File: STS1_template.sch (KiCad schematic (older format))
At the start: 9 parts, among them U1 coordinate_system

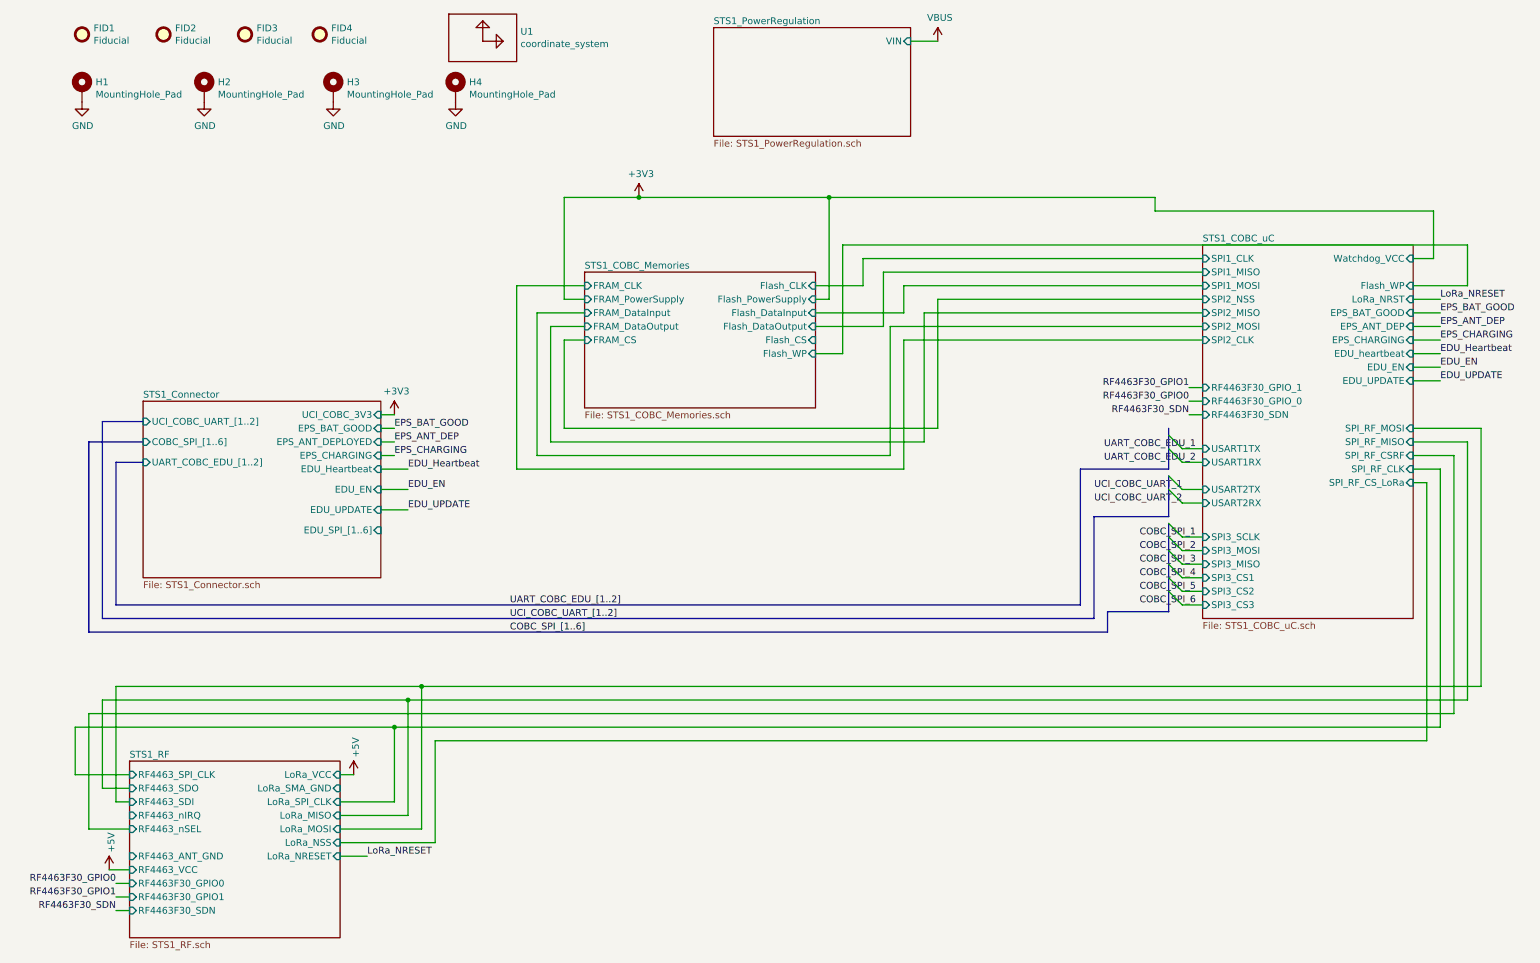
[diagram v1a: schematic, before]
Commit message: added powerplane + testpoints + some debugging
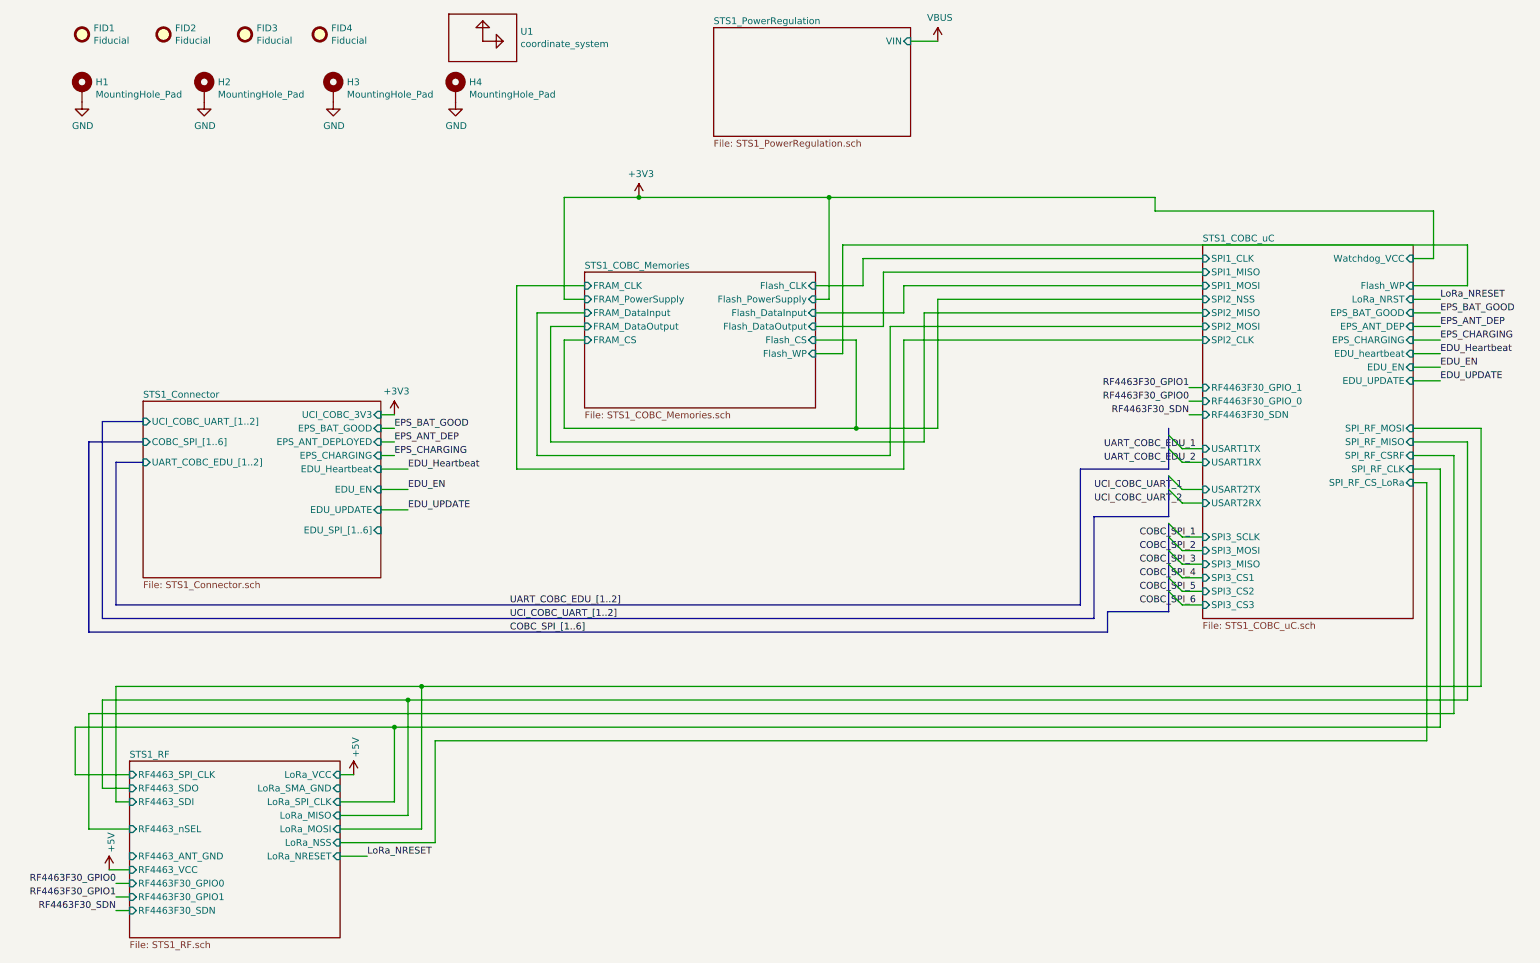
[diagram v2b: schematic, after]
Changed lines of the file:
@@
 F9 "RF4463_ANT_GND" I L 1050 6750 50
 F10 "RF4463_nSEL" I L 1050 6550 50
-F11 "RF4463_nIRQ" I L 1050 6450 50
-F12 "RF4463_SDI" I L 1050 6350 50
-F13 "RF4463_SDO" I L 1050 6250 50
-F14 "RF4463_SPI_CLK" I L 1050 6150 50
-F15 "RF4463F30_GPIO0" I L 1050 6950 50
-F16 "RF4463F30_GPIO1" I L 1050 7050 50
-F17 "LoRa_NRESET" I R 2600 6750 50
-F18 "RF4463F30_SDN" I L 1050 7150 50
+F11 "RF4463_SDI" I L 1050 6350 50
+F12 "RF4463_SDO" I L 1050 6250 50
+F13 "RF4463_SPI_CLK" I L 1050 6150 50
+F14 "RF4463F30_GPIO0" I L 1050 6950 50
+F15 "RF4463F30_GPIO1" I L 1050 7050 50
+F16 "LoRa_NRESET" I R 2600 6750 50
+F17 "RF4463F30_SDN" I L 1050 7150 50
 $EndSheet
 Wire Wire Line
@@
 	950  6350 1050 6350
 Wire Wire Line
-	7000 3600 4250 3600
+	7000 3600 6400 3600
 Wire Wire Line
 	4250 3600 4250 2950
@@
 Wire Wire Line
 	8800 4900 8950 4900
-Wire Bus Line
-	8700 3950 8700 4250
-Wire Bus Line
-	8700 3600 8700 3900
-Wire Bus Line
-	8700 4300 8700 4950
 Text Label 8900 4400 2    50   ~ 0
 COBC_SPI_1
@@
 Text Label 3850 5100 0    50   ~ 0
 COBC_SPI_[1..6]
+Wire Wire Line
+	6100 2950 6400 2950
+Wire Wire Line
+	6400 2950 6400 3600
+Wire Bus Line
+	8700 3950 8700 4250
+Wire Bus Line
+	8700 3600 8700 3900
+Wire Bus Line
+	8700 4300 8700 4950
+Connection ~ 6400 3600
+Wire Wire Line
+	6400 3600 4250 3600
 $EndSCHEMATC
